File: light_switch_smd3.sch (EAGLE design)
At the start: 17 parts

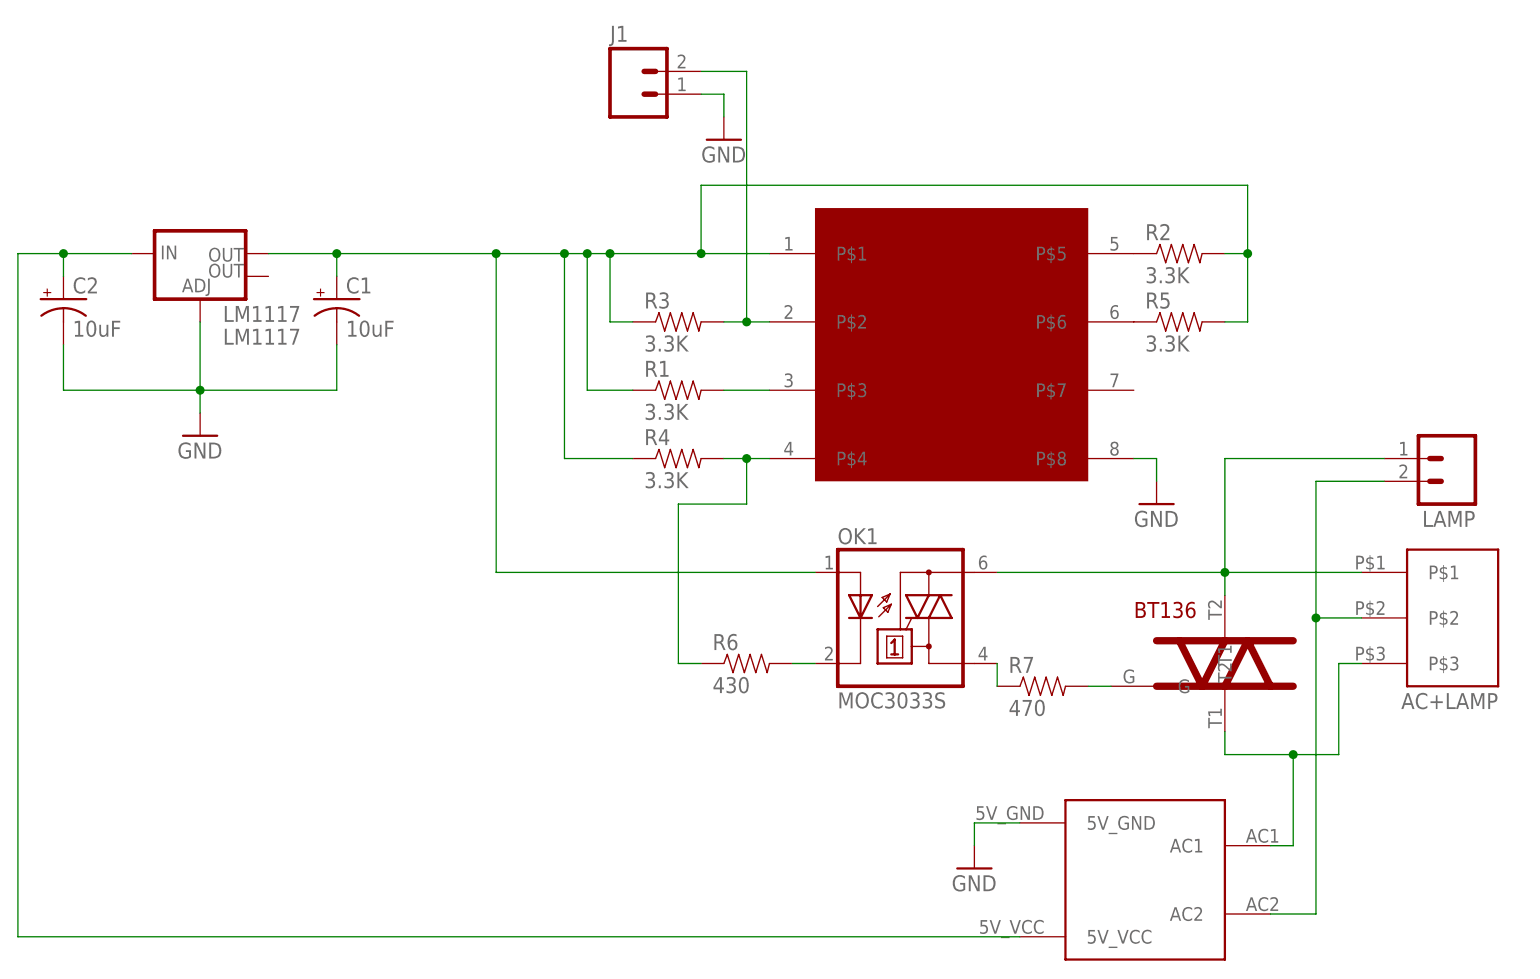
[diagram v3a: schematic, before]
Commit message: Rev 0.8 - pcb shrinked a bit.
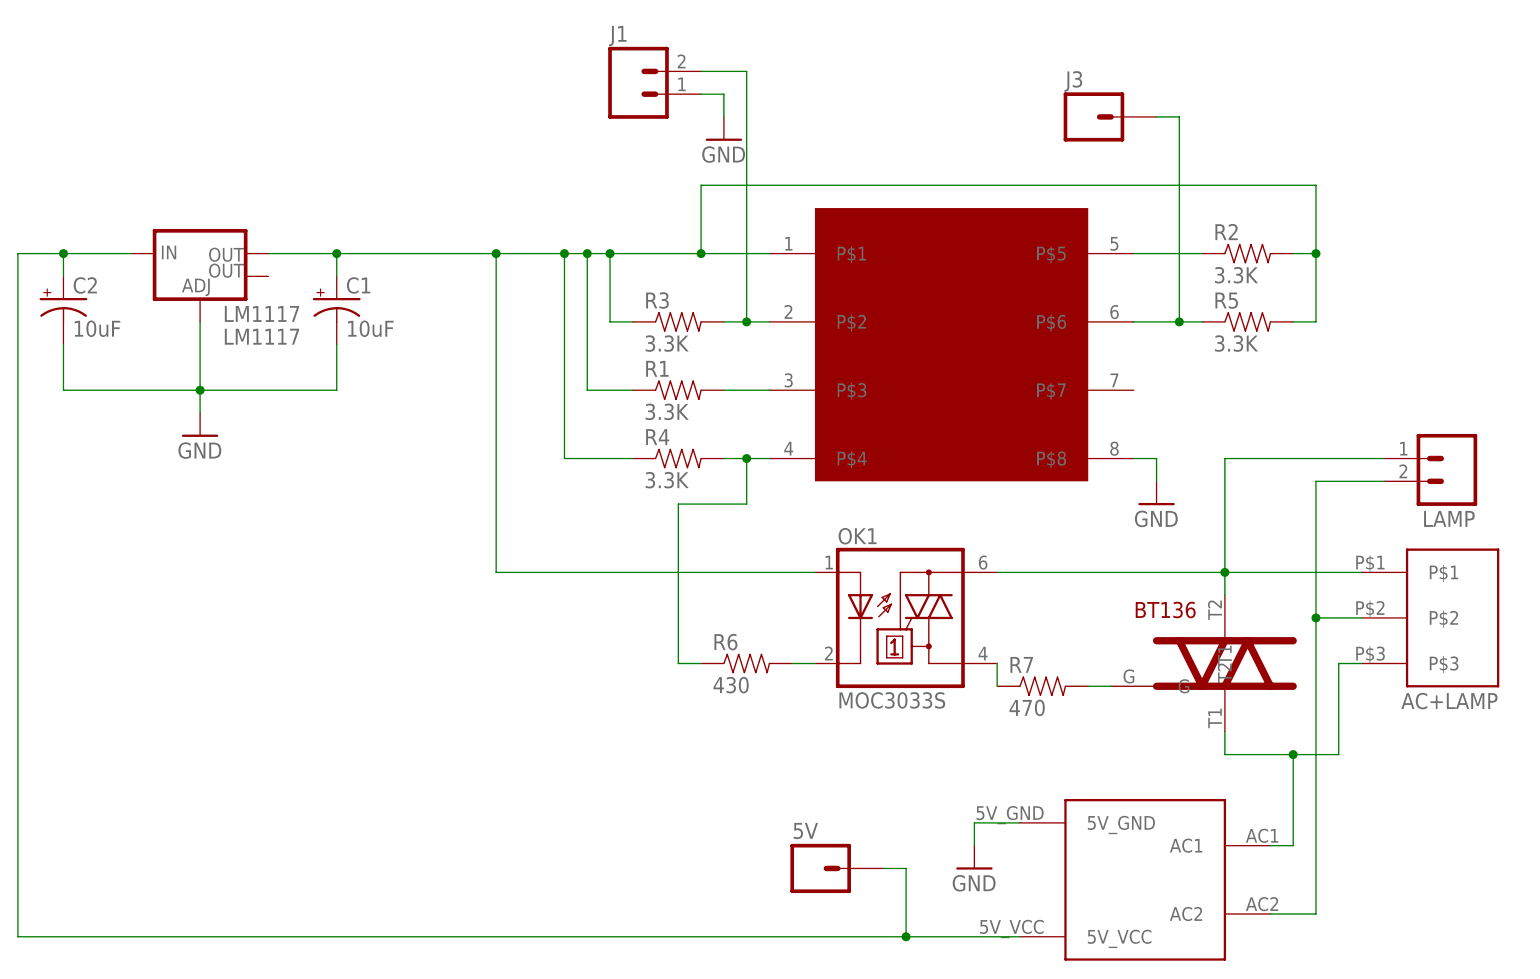
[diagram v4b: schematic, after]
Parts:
- added 5V, J3: (no value), SparkFun-Connectors:M01PTH
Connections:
- net N$13: now also 5V.1
- net N$14: now also J3.1
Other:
- moved on the sheet: R2, R5
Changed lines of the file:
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@@
 <part name="BT136" library="myblog_library" deviceset="BT136" device=""/>
 <part name="LAMP" library="SparkFun-Connectors" deviceset="M02" device="PTH"/>
+<part name="5V" library="SparkFun-Connectors" deviceset="M01" device="PTH"/>
+<part name="J3" library="SparkFun-Connectors" deviceset="M01" device="PTH"/>
 </parts>
 <sheets>
@@
 <instance part="C2" gate="G$1" x="-10.16" y="68.58"/>
 <instance part="R1" gate="G$1" x="58.42" y="58.42"/>
-<instance part="R2" gate="G$1" x="114.3" y="73.66"/>
+<instance part="R2" gate="G$1" x="121.92" y="73.66"/>
 <instance part="R3" gate="G$1" x="58.42" y="66.04"/>
 <instance part="R4" gate="G$1" x="58.42" y="50.8"/>
-<instance part="R5" gate="G$1" x="114.3" y="66.04"/>
+<instance part="R5" gate="G$1" x="121.92" y="66.04"/>
 <instance part="R6" gate="G$1" x="66.04" y="27.94"/>
 <instance part="R7" gate="G$1" x="99.06" y="25.4"/>
@@
 <instance part="BT136" gate="G$1" x="119.38" y="27.94"/>
 <instance part="LAMP" gate="G$1" x="144.78" y="50.8" rot="R180"/>
+<instance part="5V" gate="G$1" x="73.66" y="5.08"/>
+<instance part="J3" gate="G$1" x="104.14" y="88.9"/>
 </instances>
 <busses>
@@
 <wire x1="45.72" y1="50.8" x2="45.72" y2="73.66" width="0.1524" layer="91"/>
 <wire x1="60.96" y1="73.66" x2="60.96" y2="81.28" width="0.1524" layer="91"/>
-<wire x1="60.96" y1="81.28" x2="121.92" y2="81.28" width="0.1524" layer="91"/>
-<wire x1="121.92" y1="81.28" x2="121.92" y2="73.66" width="0.1524" layer="91"/>
+<wire x1="60.96" y1="81.28" x2="129.54" y2="81.28" width="0.1524" layer="91"/>
+<wire x1="129.54" y1="81.28" x2="129.54" y2="73.66" width="0.1524" layer="91"/>
 <pinref part="R2" gate="G$1" pin="2"/>
-<wire x1="121.92" y1="73.66" x2="119.38" y2="73.66" width="0.1524" layer="91"/>
+<wire x1="129.54" y1="73.66" x2="127" y2="73.66" width="0.1524" layer="91"/>
 <pinref part="R5" gate="G$1" pin="2"/>
-<wire x1="119.38" y1="66.04" x2="121.92" y2="66.04" width="0.1524" layer="91"/>
-<wire x1="121.92" y1="66.04" x2="121.92" y2="73.66" width="0.1524" layer="91"/>
+<wire x1="127" y1="66.04" x2="129.54" y2="66.04" width="0.1524" layer="91"/>
+<wire x1="129.54" y1="66.04" x2="129.54" y2="73.66" width="0.1524" layer="91"/>
 <junction x="50.8" y="73.66"/>
 <junction x="48.26" y="73.66"/>
@@
 <junction x="38.1" y="73.66"/>
 <junction x="60.96" y="73.66"/>
-<junction x="121.92" y="73.66"/>
+<junction x="129.54" y="73.66"/>
 <junction x="20.32" y="73.66"/>
 </segment>
@@
 <wire x1="-10.16" y1="73.66" x2="-10.16" y2="71.12" width="0.1524" layer="91"/>
 <pinref part="U$1" gate="G$1" pin="5V_VCC"/>
-<wire x1="96.52" y1="-2.54" x2="-15.24" y2="-2.54" width="0.1524" layer="91"/>
+<wire x1="96.52" y1="-2.54" x2="83.82" y2="-2.54" width="0.1524" layer="91"/>
+<wire x1="83.82" y1="-2.54" x2="-15.24" y2="-2.54" width="0.1524" layer="91"/>
 <wire x1="-15.24" y1="-2.54" x2="-15.24" y2="73.66" width="0.1524" layer="91"/>
 <wire x1="-15.24" y1="73.66" x2="-10.16" y2="73.66" width="0.1524" layer="91"/>
 <junction x="-10.16" y="73.66"/>
+<pinref part="5V" gate="G$1" pin="1"/>
+<wire x1="81.28" y1="5.08" x2="83.82" y2="5.08" width="0.1524" layer="91"/>
+<wire x1="83.82" y1="5.08" x2="83.82" y2="-2.54" width="0.1524" layer="91"/>
+<junction x="83.82" y="-2.54"/>
 </segment>
 </net>
@@
 <wire x1="66.04" y1="93.98" x2="66.04" y2="66.04" width="0.1524" layer="91"/>
 <junction x="66.04" y="66.04"/>
-</segment>
-</net>
-<net name="N$4" class="0">
-<segment>
-<pinref part="R1" gate="G$1" pin="2"/>
-<pinref part="U$2" gate="G$1" pin="P$3"/>
-<wire x1="63.5" y1="58.42" x2="68.58" y2="58.42" width="0.1524" layer="91"/>
 </segment>
 </net>
@@
 <pinref part="U$2" gate="G$1" pin="P$6"/>
 <pinref part="R5" gate="G$1" pin="1"/>
+<wire x1="116.84" y1="66.04" x2="114.3" y2="66.04" width="0.1524" layer="91"/>
+<pinref part="J3" gate="G$1" pin="1"/>
+<wire x1="114.3" y1="66.04" x2="109.22" y2="66.04" width="0.1524" layer="91"/>
+<wire x1="111.76" y1="88.9" x2="114.3" y2="88.9" width="0.1524" layer="91"/>
+<wire x1="114.3" y1="88.9" x2="114.3" y2="66.04" width="0.1524" layer="91"/>
+<junction x="114.3" y="66.04"/>
 </segment>
 </net>
@@
 <pinref part="U$2" gate="G$1" pin="P$5"/>
 <pinref part="R2" gate="G$1" pin="1"/>
+<wire x1="116.84" y1="73.66" x2="109.22" y2="73.66" width="0.1524" layer="91"/>
 </segment>
 </net>
@@
 </segment>
 </net>
+<net name="N$26" class="0">
+<segment>
+<pinref part="U$2" gate="G$1" pin="P$3"/>
+<pinref part="R1" gate="G$1" pin="2"/>
+<wire x1="63.5" y1="58.42" x2="68.58" y2="58.42" width="0.1524" layer="91"/>
+</segment>
+</net>
